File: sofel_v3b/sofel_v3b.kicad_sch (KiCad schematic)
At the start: 75 parts, among them J1 Pimaroni Trackball, J2 4PIN, J3 OLED, J4 Pimaroni Trackball, SW1 SW_PUSH_LED, SW10 SW_PUSH_LED, SW11 SW_PUSH_LED, SW12 SW_PUSH_LED, SW13 SW_PUSH_LED, SW14 SW_PUSH_LED, SW15 SW_PUSH_LED, SW16 SW_PUSH_LED, SW17 SW_PUSH_LED, SW18 SW_PUSH_LED, SW19 SW_PUSH_LED, SW2 SW_PUSH_LED, SW20 SW_PUSH_LED, SW21 SW_PUSH_LED, SW22 SW_PUSH_LED, SW23 SW_PUSH_LED, SW24 SW_PUSH_LED, SW25 Rotary_Encoder_Switch, SW26 SW_PUSH_LED, SW27 SW_PUSH_LED, SW28 SW_PUSH_LED, SW29 SW_PUSH_LED, SW3 SW_PUSH_LED, SW30 SW_PUSH_LED, SW4 SW_PUSH_LED, SW5 SW_PUSH_LED, SW6 SW_PUSH_LED, SW7 SW_PUSH_LED, SW8 SW_PUSH_LED, SW9 SW_PUSH_LED, U2 SN74AHCT1G125, U3 Pico

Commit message: Moved pico, updated OLED footprint
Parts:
- J3: footprint SofleChocLoud:OLED_4Pin_DS_64x128 -> ergodonk_kicad_library:OLED SSD1306 128x64 UNVERIFIED
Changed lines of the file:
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@@
       (effects (font (size 1.27 1.27)))
     )
-    (property "Footprint" "SofleChocLoud:OLED_4Pin_DS_64x128" (at 71.12 163.83 0)
+    (property "Footprint" "ergodonk_kicad_library:OLED SSD1306 128x64 UNVERIFIED" (at 71.12 163.83 0)
       (effects (font (size 1.27 1.27)) hide)
     )

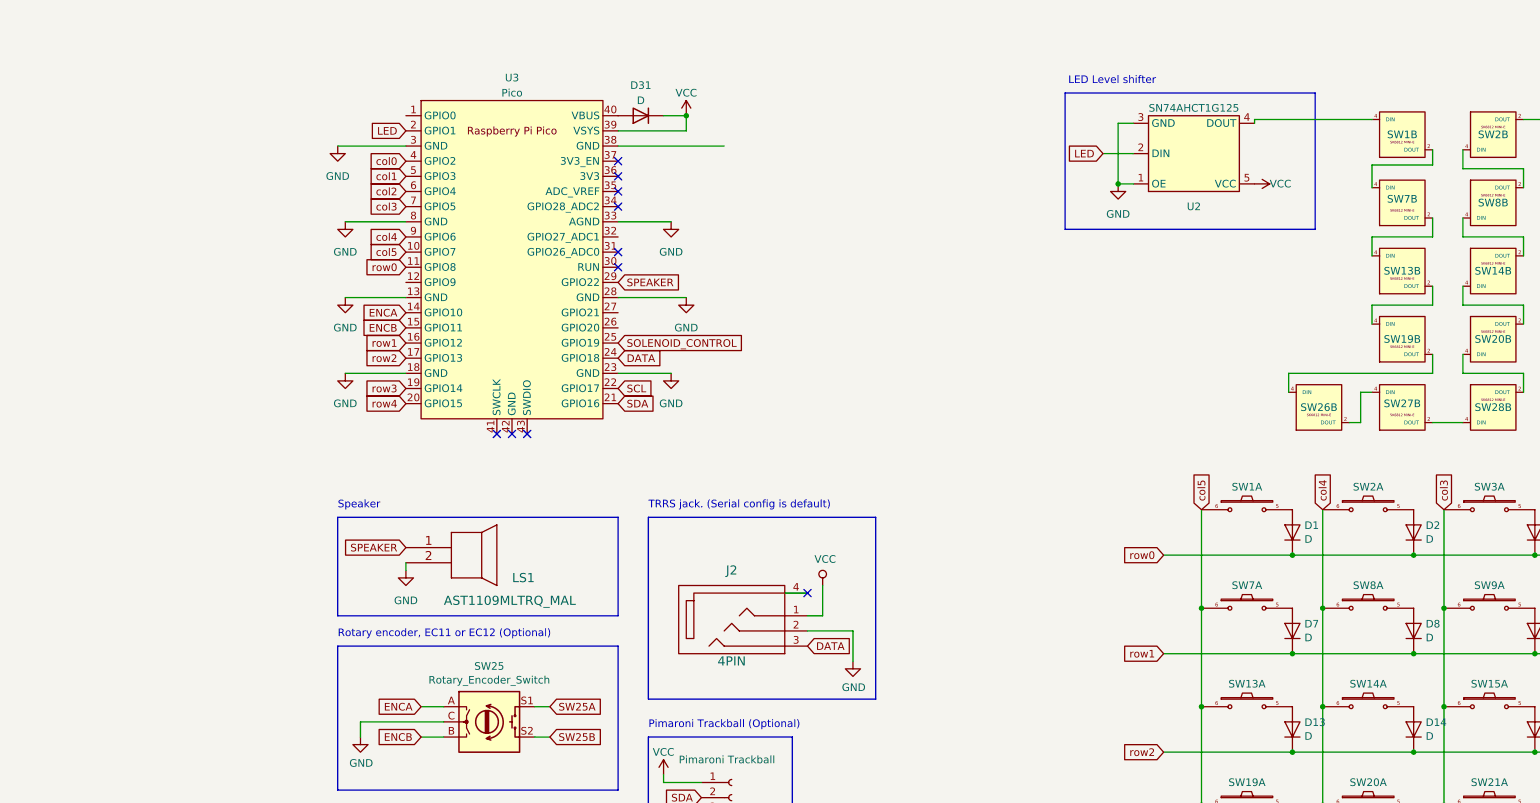
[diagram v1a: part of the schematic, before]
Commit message: Punch list fixes Removed speaker Rewired TX/RX, then back to serial Added level shifter bypass Rewired for new pico footprint
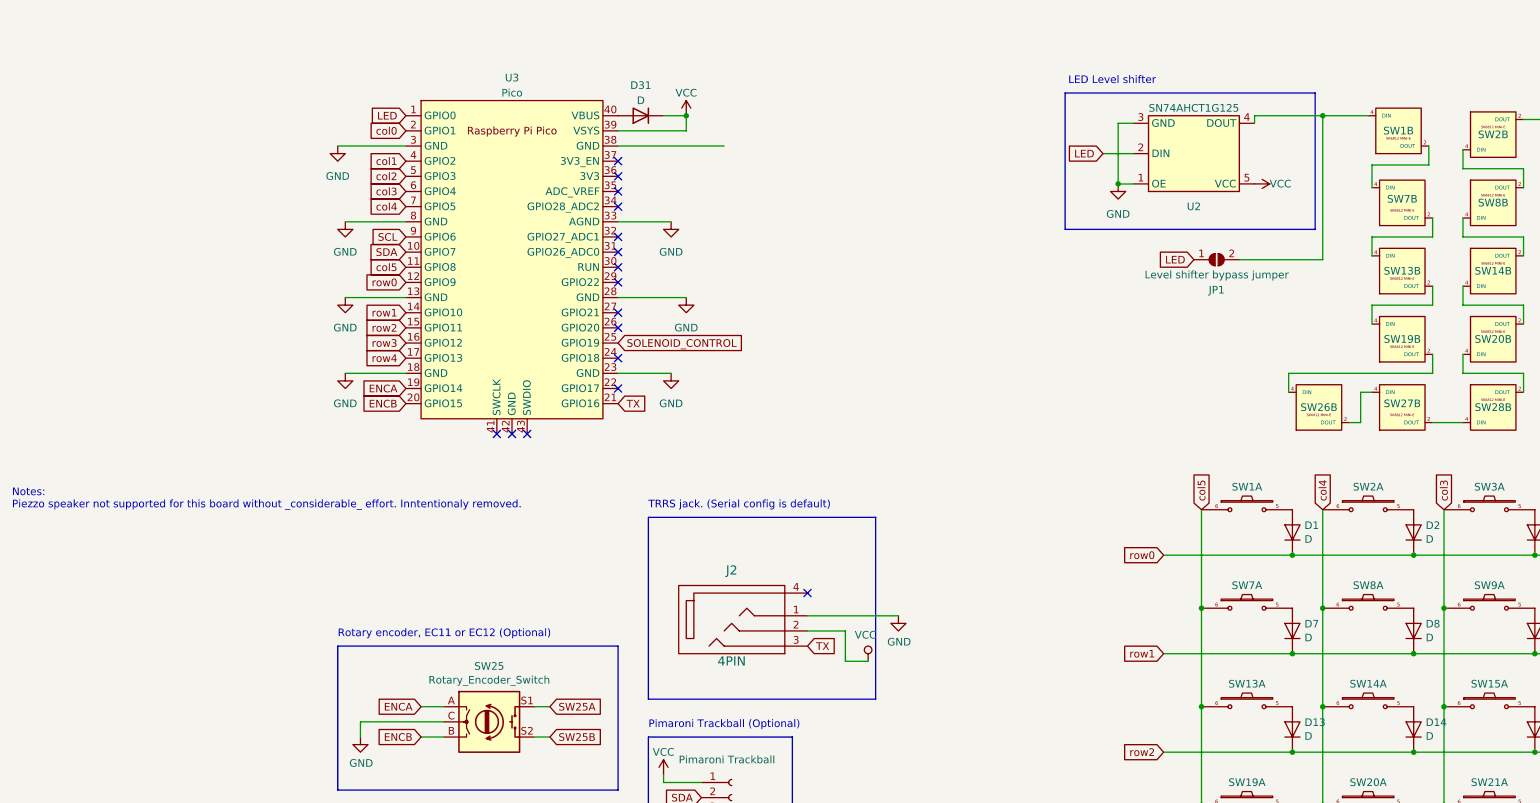
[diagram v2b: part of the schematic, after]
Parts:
- removed LS1: AST1109MLTRQ_MAL, SofleChocLoud:AST1109MLTRQ, symbol AST1109MLTRQ:AST1109MLTRQ
- added JP1: Level shifter bypass jumper, ergodonk_kicad_library:Level Shifter Bypass Jumper, symbol Jumper:SolderJumper_2_Open
- J2: footprint SofleChocLoud:TRRS_or_TRS_Sofle_Click -> ergodonk_kicad_library:MJ-4PP-9_CANTOR_KITCHEN_SINK
- U3: footprint ergodonk_kicad_library:RPi_Pico_SMD_TH - Junco -DS Sofle v3b -> ergodonk_kicad_library:RPi_Pico_SMD_TH - Junco -DS Sofle v3b v3
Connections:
- net ENCA: now also U3.19 (GPIO14); no longer U3.14 (GPIO10)
- net ENCB: now also U3.20 (GPIO15); no longer U3.15 (GPIO11)
- net GND: now also J2.1; no longer J2.2
- net LED: now also U3.1 (GPIO0), JP1.1 (A); no longer U3.2 (GPIO1)
- net SCL: now also U3.9 (GPIO6); no longer U3.22 (GPIO17)
- net SDA: now also U3.10 (GPIO7); no longer U3.21 (GPIO16)
- net SW25A: now also U3.11 (GPIO8); no longer U3.10 (GPIO7)
- net VCC: now also J2.2; no longer J2.1
- net col0: now also U3.2 (GPIO1); no longer U3.4 (GPIO2)
- net col1: now also U3.4 (GPIO2); no longer U3.5 (GPIO3)
- net col2: now also U3.5 (GPIO3); no longer U3.6 (GPIO4)
- net col3: now also U3.6 (GPIO4); no longer U3.7 (GPIO5)
- net col4: now also U3.7 (GPIO5); no longer U3.9 (GPIO6)
- net row0: now also U3.12 (GPIO9); no longer U3.11 (GPIO8)
- net row1: now also U3.14 (GPIO10); no longer U3.16 (GPIO12)
- net row2: now also U3.15 (GPIO11); no longer U3.17 (GPIO13)
- net row3: now also U3.16 (GPIO12); no longer U3.19 (GPIO14)
- net row4: now also U3.17 (GPIO13); no longer U3.20 (GPIO15)
- net at SW1.4 (DIN), U2.4 (DOUT): now also JP1.2 (B)
- net DATA: no longer names the net of U3.24 (GPIO18)
- net DATA: no longer J2.3
- net SPEAKER: no longer names the net of U3.29 (GPIO22)
- new net TX: J2.3, U3.21 (GPIO16)
- no-connect marks 13 -> 19
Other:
- note added: "Notes: Piezzo speaker not supported for this board without _considerable_ effort. Inntentionaly removed."
- note removed: "Speaker"
- moved on the sheet: SW1B

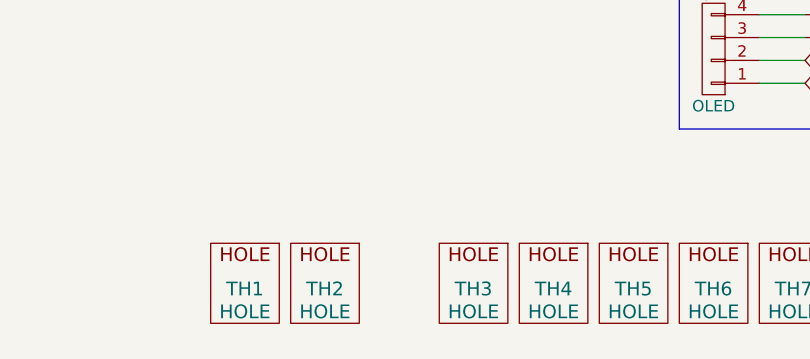
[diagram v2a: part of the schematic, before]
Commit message: minimized pimoroni footprint
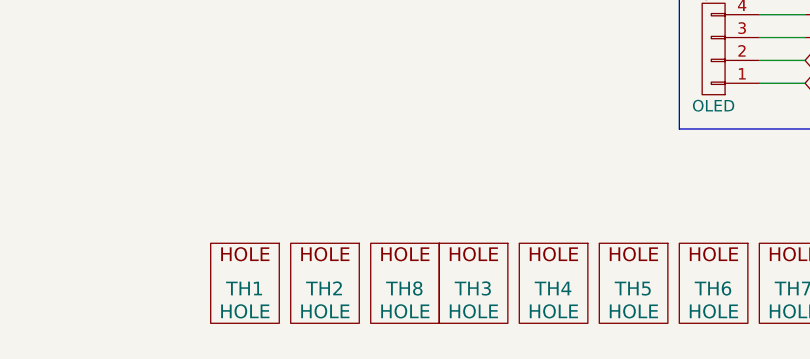
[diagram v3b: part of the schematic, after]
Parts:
- added TH8: HOLE, SofleChocLoud:Hole from sofle for M2 posts gold rimmer, symbol SofleKeyboard-rescue:HOLE-Lily58-cache-Lily58_Pro-rescue
- J1: footprint SofleChocLoud:pimoroni_trackball -> ergodonk_kicad_library:Pimaroni_PinHeader_1x05_P2.54mm_Vertical Sofle v3b
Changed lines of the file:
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@@
       (effects (font (size 1.27 1.27)) (justify left))
     )
-    (property "Footprint" "SofleChocLoud:pimoroni_trackball" (at 81.28 138.43 0)
+    (property "Footprint" "ergodonk_kicad_library:Pimaroni_PinHeader_1x05_P2.54mm_Vertical Sofle v3b" (at 81.28 138.43 0)
       (effects (font (size 1.27 1.27)) hide)
     )
@@
         )
       )
+    )
+  )
+  (symbol (lib_id "SofleKeyboard-rescue:HOLE-Lily58-cache-Lily58_Pro-rescue") (at 36.83 190.5 0) (unit 1)
+    (in_bom yes) (on_board yes) (dnp no)
+    (property "Reference" "TH8" (at 36.83 190.5 0)
+      (effects (font (size 1.524 1.524)))
+    )
+    (property "Value" "HOLE" (at 36.83 193.04 0)
+      (effects (font (size 1.524 1.524)))
+    )
+    (property "Footprint" "SofleChocLoud:Hole from sofle for M2 posts gold rimmer" (at 36.83 190.5 0)
+      (effects (font (size 1.524 1.524)) hide)
+    )
+    (property "Datasheet" "" (at 36.83 190.5 0)
+      (effects (font (size 1.524 1.524)))
+    )
+    (instances
+      (project "sofel_v3b"
+        (path "/06057b3a-55ab-4f4e-913e-2aeec5ff3587"
+          (reference "TH8") (unit 1)
+        )
+      )

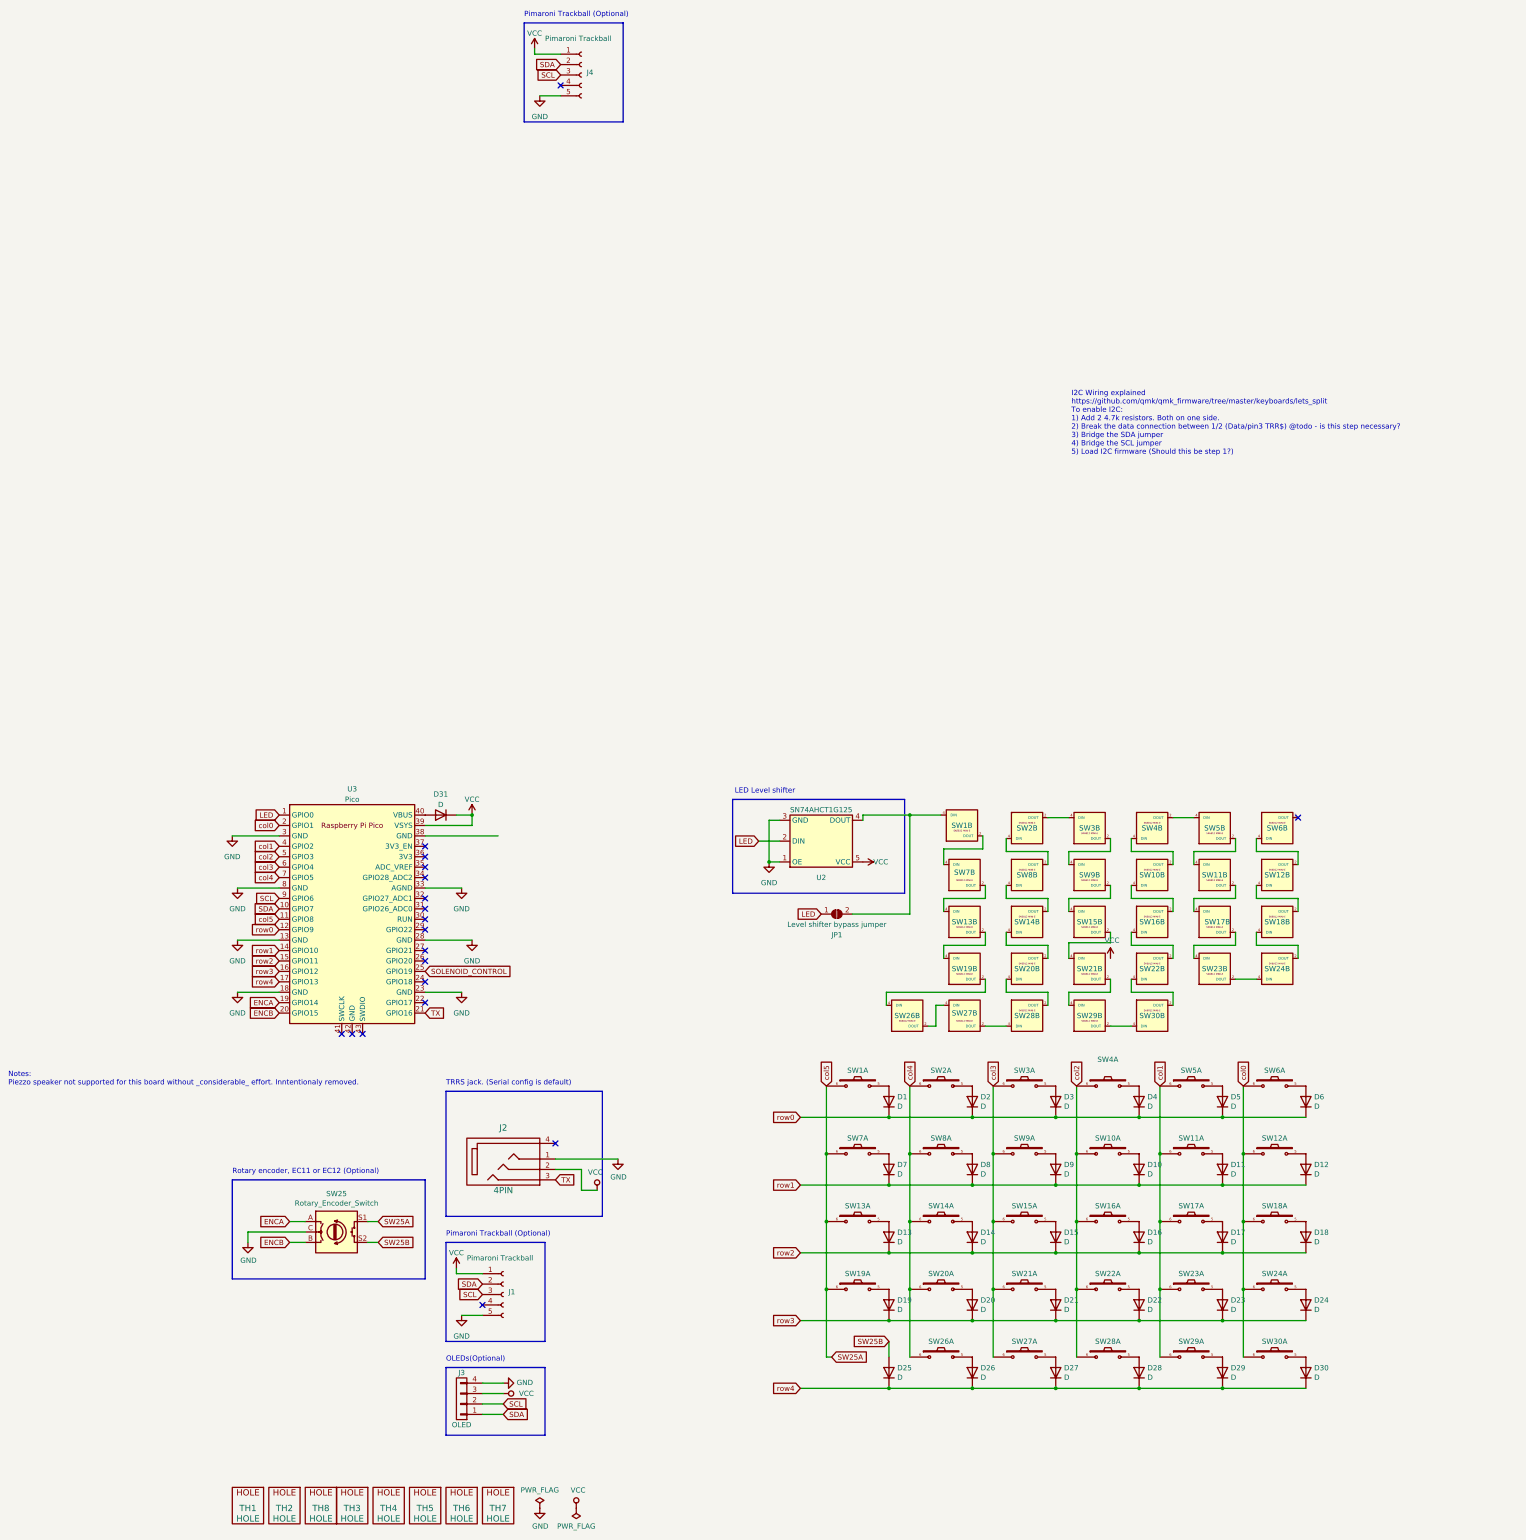
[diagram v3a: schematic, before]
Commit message: Moved footprints into repo
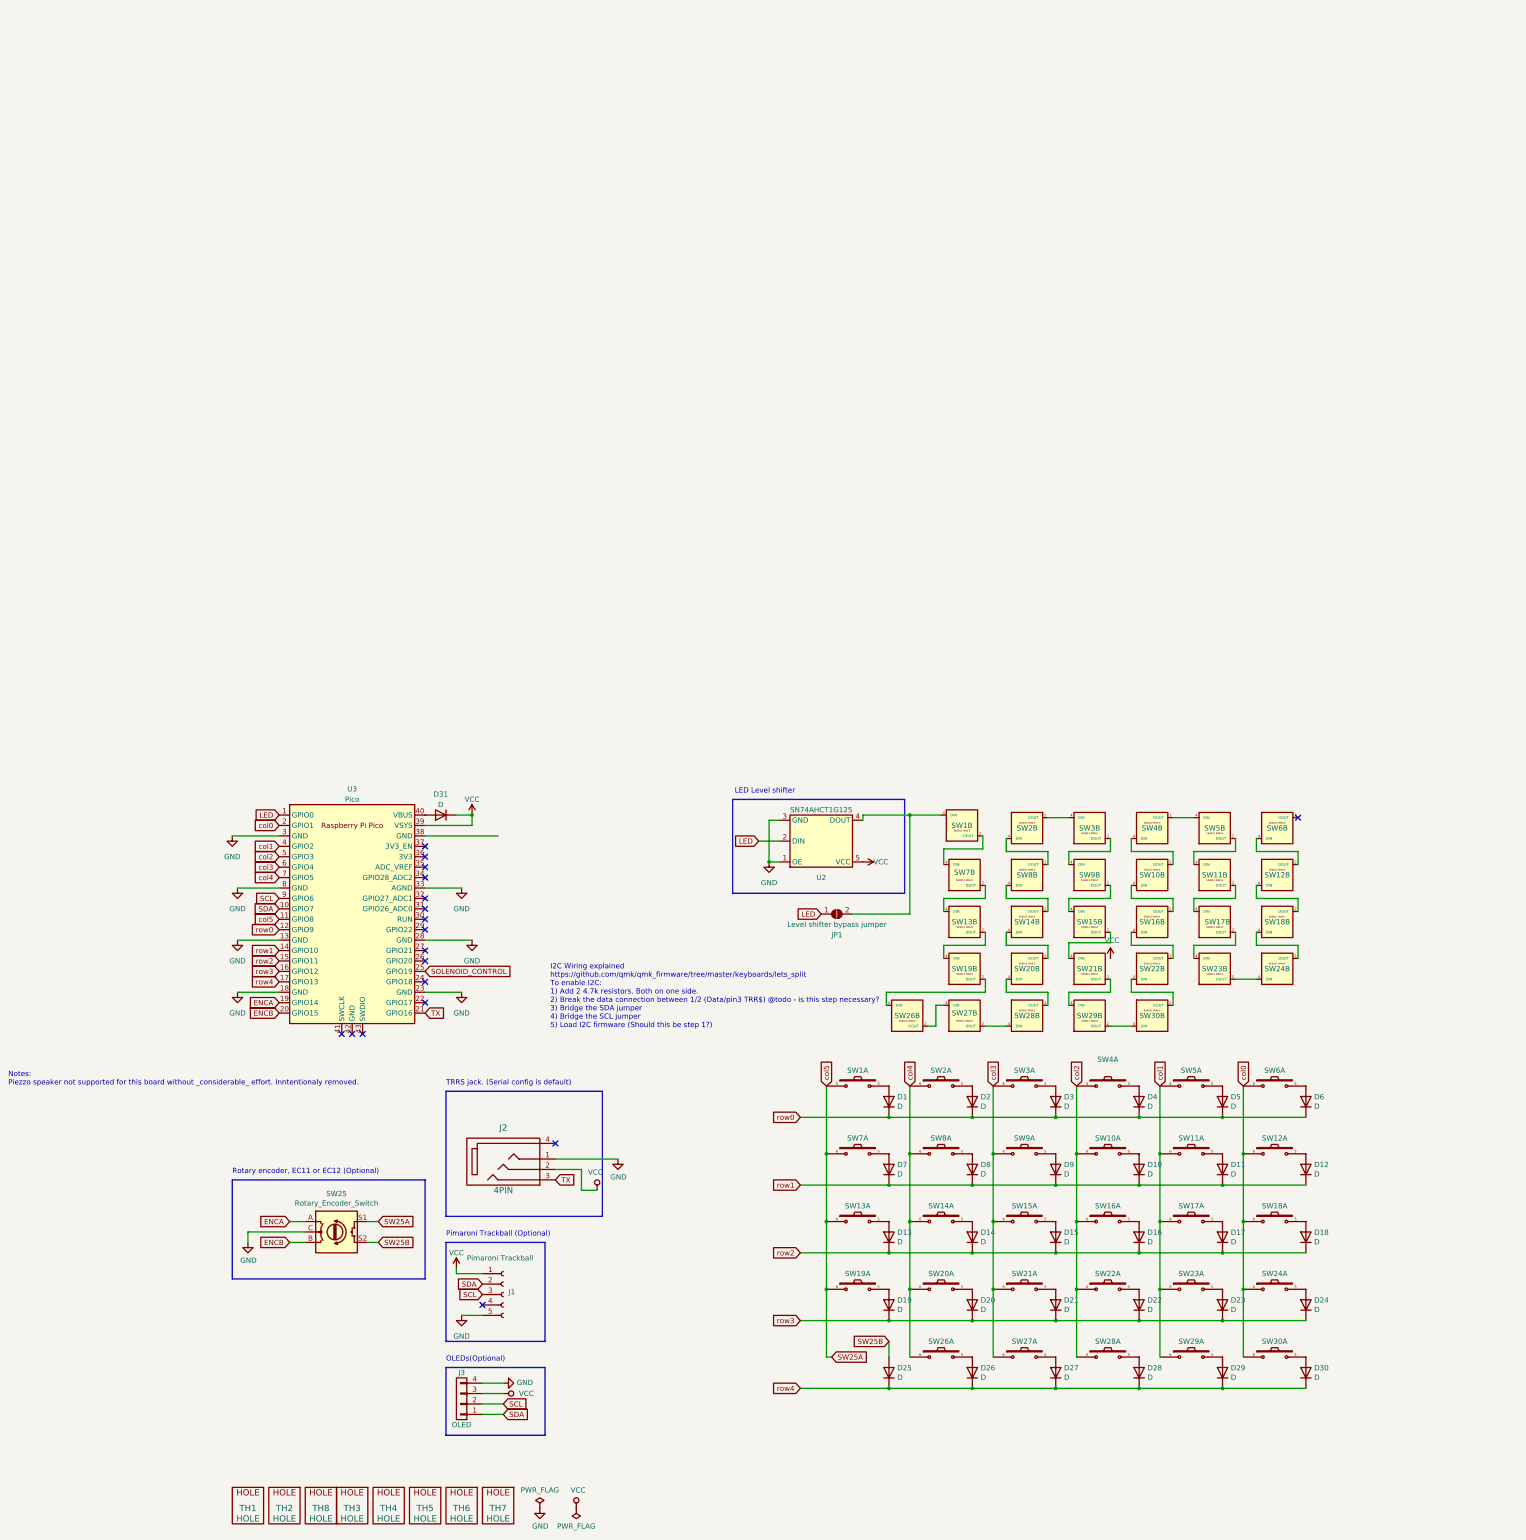
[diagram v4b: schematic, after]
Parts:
- removed J4: Pimaroni Trackball, Sofle_v3:pimoroni_trackball_breakout, symbol Connector:Conn_01x05_Socket
- D1, D10, D11, D12, D13, D14, D15, D16, D17, D18, D19, D2, D20, D21, D22, D23, D24, D25, D26, D27, D28, D29, D3, D30, D31, D4, D5, D6, D7, D8, D9: footprint SofleChocLoud:D_SOD-123_DO-35_Hybrid_DoubleSided_V2 -> sofle_v3b:D_SOD-123_DO-35_Hybrid_DoubleSided_V2
- J1: footprint ergodonk_kicad_library:Pimaroni_PinHeader_1x05_P2.54mm_Vertical Sofle v3b -> sofle_v3b:Pimaroni_PinHeader_1x05_P2.54mm_Vertical Sofle v3b
- J2: footprint ergodonk_kicad_library:MJ-4PP-9_CANTOR_KITCHEN_SINK -> sofle_v3b:MJ-4PP-9
- J3: footprint ergodonk_kicad_library:OLED SSD1306 128x64 UNVERIFIED -> sofle_v3b:OLED SSD1306 128x64 UNVERIFIED
- JP1: footprint ergodonk_kicad_library:Level Shifter Bypass Jumper -> sofle_v3b:Level Shifter Bypass Jumper
- SW1, SW10, SW11, SW12, SW13, SW14, SW15, SW16, SW17, SW18, SW19, SW2, SW20, SW21, SW22, SW23, SW24, SW26, SW27, SW28, SW29, SW3, SW30, SW4, SW5, SW6, SW7, SW8, SW9: footprint SofleChocLoud:Cherry_MX_DS_Hotswap_miniE_1U -> sofle_v3b:Cherry_MX_DS_Hotswap_miniE_1U
- SW25: footprint SofleChocLoud:RotaryEncoder_Alps_EC11E-Switch_Vertical_H20mm-keebio_modified -> sofle_v3b:RotaryEncoder_Alps_EC11E-Switch_Vertical_H20mm-keebio_modified
- TH2, TH3, TH4, TH5, TH6, TH7, TH8: footprint SofleChocLoud:Hole from sofle for M2 posts gold rimmer -> sofle_v3b:Hole from sofle for M2 posts gold rimmer
- U2: footprint ergodonk_kicad_library:SN74AHCT1G125 - Junco -> sofle_v3b:SN74AHCT1G125 - Junco
- U3: footprint ergodonk_kicad_library:RPi_Pico_SMD_TH - Junco -DS Sofle v3b v3 -> sofle_v3b:RPi_Pico_SMD_TH - Junco -DS Sofle v3b v3
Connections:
- no-connect marks 19 -> 18
